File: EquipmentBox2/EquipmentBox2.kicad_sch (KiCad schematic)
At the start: 11 parts, among them J1 UAC16-8, J10 UAC20-5, J11 UAC20-5, J2 UAC16-8, J3 UAC16-8, J4 UAC16-8, J5 UAC16-8, J6 UAC16-8, J7 UAC16-9, J8 UAC16-9, J9 UAC16-9

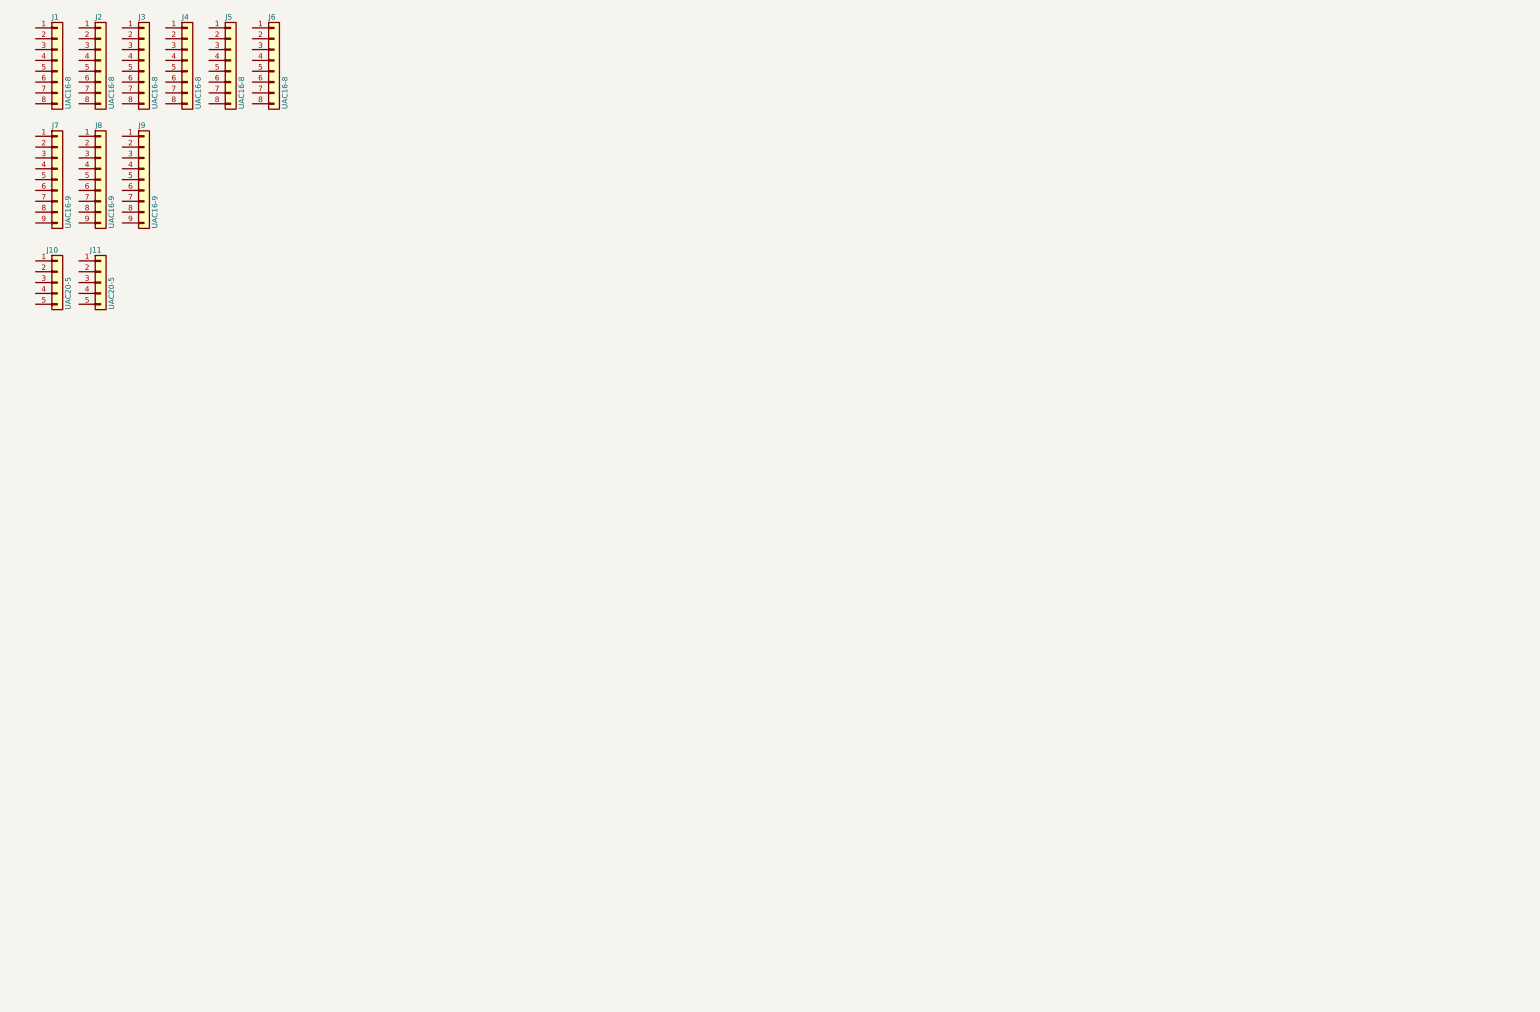
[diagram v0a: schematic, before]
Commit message: 已打样测试两版，第三版暂未修改
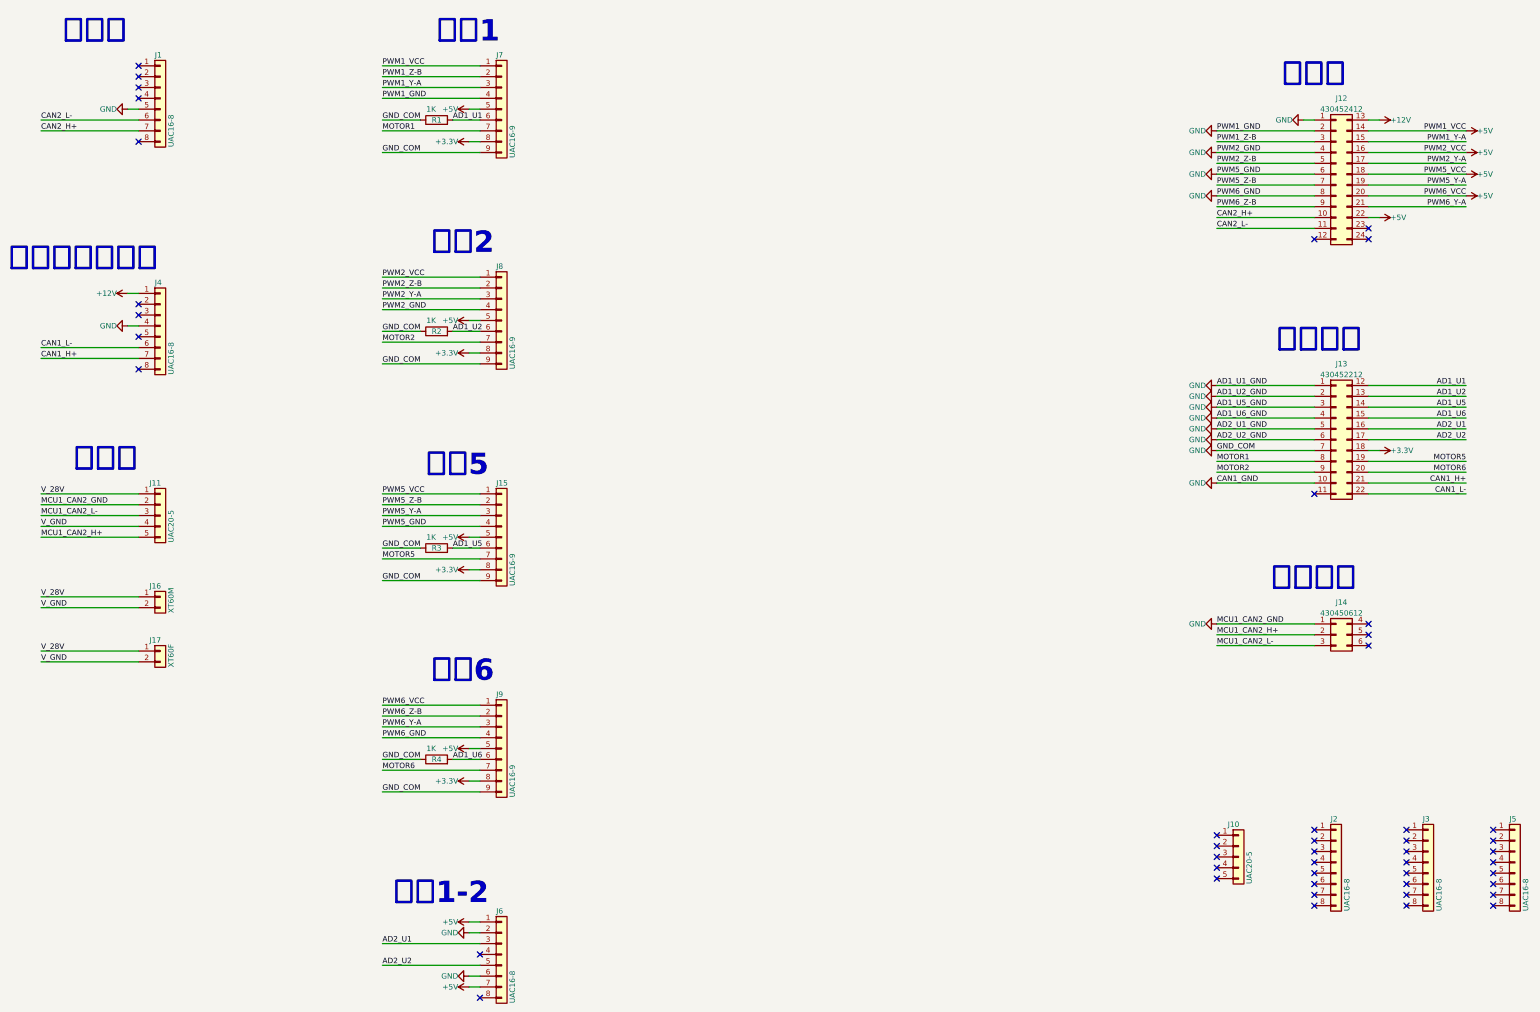
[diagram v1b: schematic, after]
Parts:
- added J12: 430452412, Molex:430452412, symbol Connector_Generic:Conn_02x12_Top_Bottom
- added J13: 430452212, Molex:430452212, symbol Connector_Generic:Conn_02x11_Top_Bottom
- added J14: 430450612, Molex:430450612, symbol Connector_Generic:Conn_02x03_Top_Bottom
- added J15: UAC16-9, UACsocket:UAC16-9, symbol Connector_Generic:Conn_01x09
- added J16: XT60M, Connector_AMASS:AMASS_XT60-M_1x02_P7.20mm_Vertical, symbol Connector_Generic:Conn_01x02
- added J17: XT60F, Connector_AMASS:AMASS_XT60-F_1x02_P7.20mm_Vertical, symbol Connector_Generic:Conn_01x02
- added R1, R2, R3, R4: 1K, Resistor_SMD:R_0402_1005Metric, symbol Device:R
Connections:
- net +5V: now reaches J6.1 (Pin_1)
- net +5V: now also J6.7 (Pin_7), J7.1 (Pin_1), J7.5 (Pin_5), J8.1 (Pin_1), J8.5 (Pin_5), J9.1 (Pin_1), J9.5 (Pin_5), J12.14 (Pin_14), J12.16 (Pin_16), J12.18 (Pin_18), J12.20 (Pin_20), J12.22 (Pin_22), J15.1 (Pin_1), J15.5 (Pin_5)
- net GND: now reaches J6.2 (Pin_2)
- net GND: now also J1.5 (Pin_5), J11.2 (Pin_2), J4.4 (Pin_4), J6.6 (Pin_6), J7.4 (Pin_4), J7.9 (Pin_9), J8.4 (Pin_4), J8.9 (Pin_9), J9.4 (Pin_4), J9.9 (Pin_9), J12.1 (Pin_1), J12.2 (Pin_2), J12.4 (Pin_4), J12.6 (Pin_6), J12.8 (Pin_8), J13.1 (Pin_1), J13.10 (Pin_10), J13.2 (Pin_2), J13.3 (Pin_3), J13.4 (Pin_4), J13.5 (Pin_5), J13.6 (Pin_6), J13.7 (Pin_7), J14.1 (Pin_1), J15.4 (Pin_4), J15.9 (Pin_9), R1.1, R2.1, R3.1, R4.1
- net AD2_U1: now reaches J6.3 (Pin_3)
- net AD2_U1: now also J13.16 (Pin_16)
- net AD2_U2: now reaches J6.5 (Pin_5)
- net AD2_U2: now also J13.17 (Pin_17)
- net CAN2_L-: now reaches J1.6 (Pin_6)
- net CAN2_L-: now also J12.11 (Pin_11)
- net CAN2_H+: now reaches J1.7 (Pin_7)
- net CAN2_H+: now also J12.10 (Pin_10)
- net PWM2_Z-B: now reaches J8.2 (Pin_2)
- net PWM2_Z-B: now also J12.5 (Pin_5)
- net PWM2_Y-A: now reaches J8.3 (Pin_3)
- net PWM2_Y-A: now also J12.17 (Pin_17)
- net AD1_U2: now reaches J8.6 (Pin_6)
- net AD1_U2: now also J13.13 (Pin_13), R2.2
- net MOTOR2: now reaches J8.7 (Pin_7)
- net MOTOR2: now also J13.9 (Pin_9)
- net +3.3V: now reaches J8.8 (Pin_8)
- net +3.3V: now also J7.8 (Pin_8), J9.8 (Pin_8), J13.18 (Pin_18), J15.8 (Pin_8)
- net V_28V: now reaches J11.1 (Pin_1)
- net V_28V: now also J16.1 (Pin_1), J17.1 (Pin_1)
- net MCU1_CAN2_L-: now reaches J11.3 (Pin_3)
- net MCU1_CAN2_L-: now also J14.3 (Pin_3)
- net V_GND: now reaches J11.4 (Pin_4)
- net V_GND: now also J16.2 (Pin_2), J17.2 (Pin_2)
- net MCU1_CAN2_H+: now reaches J11.5 (Pin_5)
- net MCU1_CAN2_H+: now also J14.2 (Pin_2)
- net PWM6_Z-B: now reaches J9.2 (Pin_2)
- net PWM6_Z-B: now also J12.9 (Pin_9)
- net PWM6_Y-A: now reaches J9.3 (Pin_3)
- net PWM6_Y-A: now also J12.21 (Pin_21)
- net AD1_U6: now reaches J9.6 (Pin_6)
- net AD1_U6: now also J13.15 (Pin_15), R4.2
- net MOTOR6: now reaches J9.7 (Pin_7)
- net MOTOR6: now also J13.20 (Pin_20)
- net PWM1_Z-B: now reaches J7.2 (Pin_2)
- net PWM1_Z-B: now also J12.3 (Pin_3)
- net PWM1_Y-A: now reaches J7.3 (Pin_3)
- net PWM1_Y-A: now also J12.15 (Pin_15)
- net AD1_U1: now reaches J7.6 (Pin_6)
- net AD1_U1: now also J13.12 (Pin_12), R1.2
- net MOTOR1: now reaches J7.7 (Pin_7)
- net MOTOR1: now also J13.8 (Pin_8)
- net +12V: now reaches J4.1 (Pin_1)
- net +12V: now also J12.13 (Pin_13)
- net CAN1_L-: now reaches J4.6 (Pin_6)
- net CAN1_L-: now also J13.22 (Pin_22)
- net CAN1_H+: now reaches J4.7 (Pin_7)
- net CAN1_H+: now also J13.21 (Pin_21)
- new net AD1_U5: J13.14 (Pin_14), J15.6 (Pin_6), R3.2
- new net MOTOR5: J13.19 (Pin_19), J15.7 (Pin_7)
- new net PWM5_Y-A: J12.19 (Pin_19), J15.3 (Pin_3)
- new net PWM5_Z-B: J12.7 (Pin_7), J15.2 (Pin_2)
- no-connect marks 0 -> 47
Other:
- note added: "倾转1-2"
- note added: "左机翼"
- note added: "电调1"
- note added: "电调2"
- note added: "电调5"
- note added: "电调6"
- note added: "调试口"
- note added: "转发板左"
- note added: "采集板左"
- note added: "雷达、电池接口"
- note added: "飞控左"
- company: (none) -> 南京拓兴智控
- title: (none) -> 设备盒PCB2
- moved on the sheet: J1, J10, J11, J2, J3, J4, J5, J6, J7, J8, J9
